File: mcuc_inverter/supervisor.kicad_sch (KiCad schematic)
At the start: 0 parts

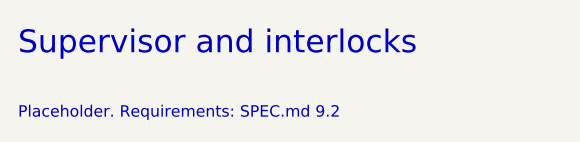
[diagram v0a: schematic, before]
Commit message: Design the supervisor interlock block
Adds docs/supervisor.md: the full logic design for the firmware-independent
hardware interlocks required by SPEC.md §9.2 -- overcurrent detect and latch,
fault aggregation, PWM overlap elimination and dead time. Includes the
24-signal interface, gate budget, and a failure-mode review done on the
assumption that firmware is hostile.

Two selections differ from the original PALTA board, both deliberate:

- Comparators run from +5 V, not 3.3 V. The LM2903's input common-mode
  ceiling is VCC-1.5V, so on 3.3 V it is 1.8 V -- below the 3.05 V positive
  trip point. The positive-overcurrent channel would never have asserted.
  Open-drain outputs still pull up to 3.3 V, so no level shifting is needed.
- 74HC replaces 74ACT. The dead-time RC assumes a CMOS threshold at
  0.5*VCC; 74ACT's TTL thresholds make the delay supply- and part-dependent.
  Predictable dead time beats ~10 ns of propagation delay here.

Adds tools/gen_skeleton.py, which generates the KiCad skeleton and records
the block interfaces, and ERC severities in mcuc_inverter.kicad_pro:
hier_label_mismatch stays an error, label_dangling and pin_not_connected
become warnings during build-out.

The interface is not emitted into the schematic yet (EMIT_INTERFACE=False).
Emitting it into empty sheets produces 96 legitimate dangling-label
violations, and copperhead check fails on warnings as well as errors, which
would leave the verification gate permanently red -- the same failure mode
that let the earlier generated documents through unchecked. The interface
lands in the same change as the components. Rationale in supervisor.md §9.

Verified: kicad-cli sch erc reports 0 violations and copperhead check is
green. With the interface temporarily emitted, ERC reported no
hier_label_mismatch, confirming all 24 names and directions agree across
every sheet boundary.

Co-Authored-By: Claude Opus 5 <noreply@anthropic.com>
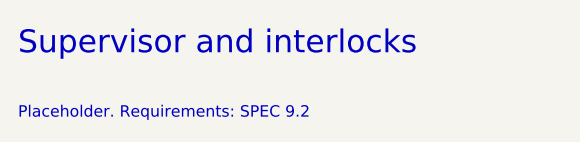
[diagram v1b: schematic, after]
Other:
- note added: "Placeholder. Requirements: SPEC 9.2"
- note removed: "Placeholder. Requirements: SPEC.md 9.2"
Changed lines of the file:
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@@
 		)
 	)
-	(text "Placeholder. Requirements: SPEC.md 9.2"
+	(text "Placeholder. Requirements: SPEC 9.2"
 		(exclude_from_sim no)
 		(at 20 27 0)

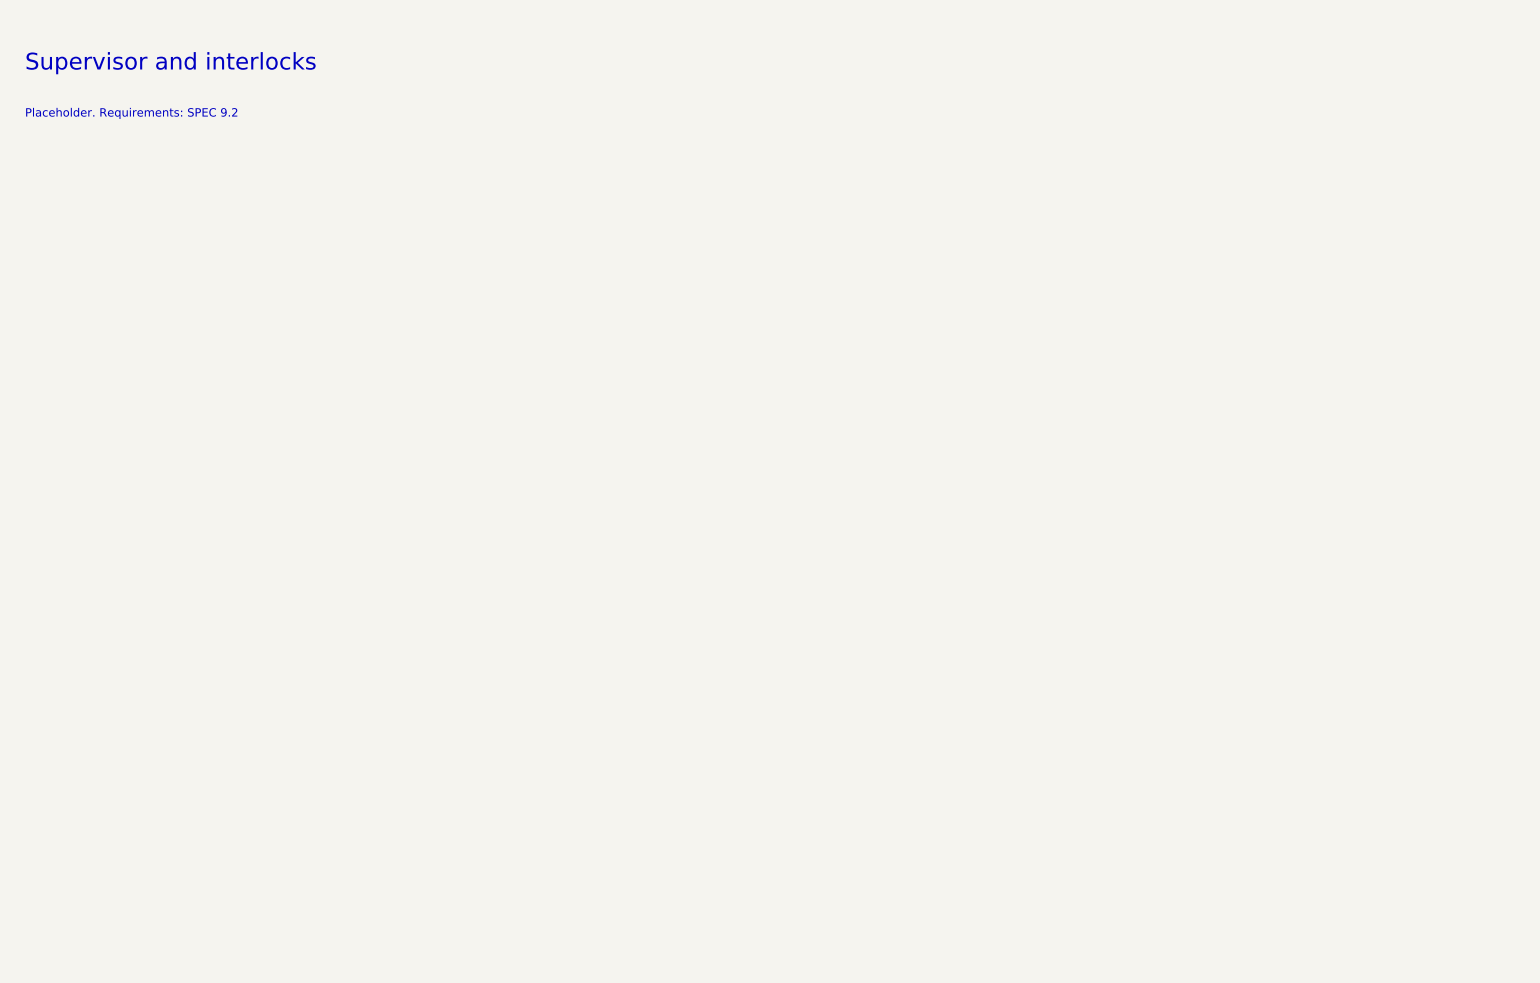
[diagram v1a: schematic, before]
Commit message: Place the supervisor overcurrent comparator front end
Implements docs/supervisor.md section 3 in the schematic: 13 components
across the threshold divider, six LM2903 comparator channels and the
wired-OR trip node.

A single three-resistor string (1k / 11k / 1k off +3V3) generates both
thresholds -- 3.046 V and 0.254 V, i.e. +/-280 A -- which keeps them
ratiometric with the rail the current sense is referenced to, so divider
tolerance and rail drift track out of the trip point.

Channel polarity: the positive trip puts V_TH_POS on IN+ and ISENSE on
IN-, the negative trip the other way round, so both pull the open-drain
output low on an overcurrent of either sign. All six outputs wire-OR onto
OC_TRIP_N with one 4.7k pull-up to +3V3 and a 100 pF filter.

Verified by netlist export rather than assumption:
  OC_TRIP_N  8 nodes  six comparator outputs + pull-up + filter
  V_TH_POS   6 nodes  divider tap, decoupling, three positive-channel IN+
  V_TH_NEG   6 nodes  divider tap, decoupling, three negative-channel IN-
  ISENSE_x   2 nodes  Ux.2 and Ux.5, the intended cross-pairing
  +5V        6 nodes  three LM2903 V+ and three decoupling caps
  GND       10 nodes
ERC reports 0 errors.

gen_skeleton.py now emits interface signals selectively via EMIT_SIGNALS
instead of all-or-nothing, so warnings stay proportional to what is built.
Six warnings remain -- 3 label_dangling and 3 pin_not_driven -- all saying
that current_sense does not exist yet so nothing drives ISENSE. Left in
place deliberately; they clear when that block is populated.

pin_not_driven joins the WIP warning severities. hier_label_mismatch stays
an error, since a boundary mismatch is a real defect at any build state.

Note that copperhead check fails on warnings as well as errors, so it reads
red while any block is unbuilt. kicad-cli sch erc --severity-error is the
meaningful gate during build-out and currently reports 0.

Co-Authored-By: Claude Opus 5 <noreply@anthropic.com>
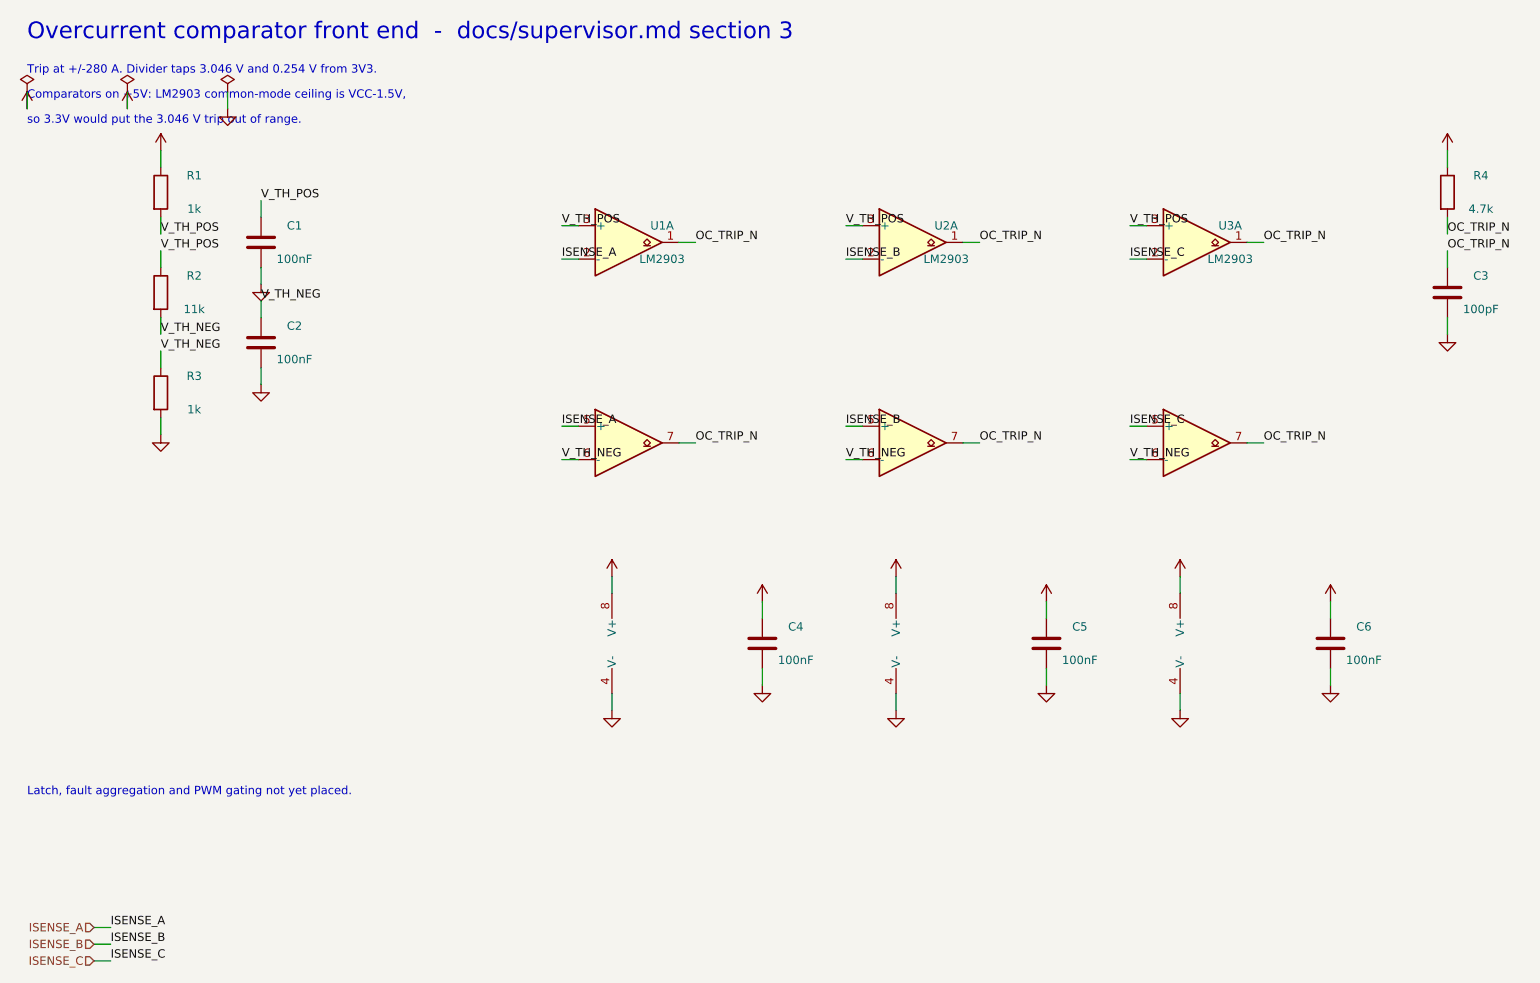
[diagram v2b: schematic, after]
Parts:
- added C1, C2, C4, C5, C6: 100nF, symbol Device:C
- added C3: 100pF, symbol Device:C
- added R1, R3: 1k, symbol Device:R
- added R2: 11k, symbol Device:R
- added R4: 4.7k, symbol Device:R
- added U1, U2, U3: LM2903, symbol Comparator:LM2903
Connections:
- new net +3V3: R1.1, R4.1
- new net +5V: C4.1, C5.1, C6.1, U1.8 (V+), U2.8 (V+), U3.8 (V+)
- new net GND: C1.2, C2.2, C3.2, C4.2, C5.2, C6.2, R3.2, U1.4 (V-), U2.4 (V-), U3.4 (V-)
- new net ISENSE_A: U1.2 (-), U1.5 (+)
- new net ISENSE_B: U2.2 (-), U2.5 (+)
- new net ISENSE_C: U3.2 (-), U3.5 (+)
- new net OC_TRIP_N: C3.1, R4.2, U1.1, U1.7, U2.1, U2.7, U3.1, U3.7
- new net V_TH_NEG: C2.1, R2.2, R3.1, U1.6 (-), U2.6 (-), U3.6 (-)
- new net V_TH_POS: C1.1, R1.2, R2.1, U1.3 (+), U2.3 (+), U3.3 (+)
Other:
- note added: "Comparators on +5V: LM2903 common-mode ceiling is VCC-1.5V,"
- note added: "Latch, fault aggregation and PWM gating not yet placed."
- note added: "Overcurrent comparator front end - docs/supervisor.md section 3"
- note added: "Trip at +/-280 A. Divider taps 3.046 V and 0.254 V from 3V3."
- note added: "so 3.3V would put the 3.046 V trip out of range."
- note removed: "Placeholder. Requirements: SPEC 9.2"
- note removed: "Supervisor and interlocks"
